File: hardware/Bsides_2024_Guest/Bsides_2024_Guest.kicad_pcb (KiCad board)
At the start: 2 copper layers, 134.5 x 129.5 mm, 45 parts, among them J1 Add_On, J2 Battery, J3 Battery, J4 OLED, J5 Conn_01x05, J6 Conn_01x05, P1 USB_C_Plug_USB2.0, Q1 DMG3415U-7, SW1 ON, SW2 RESET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

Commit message: feat(Hw): Update PCB
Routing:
- added copper zone on F.Cu, net (none)

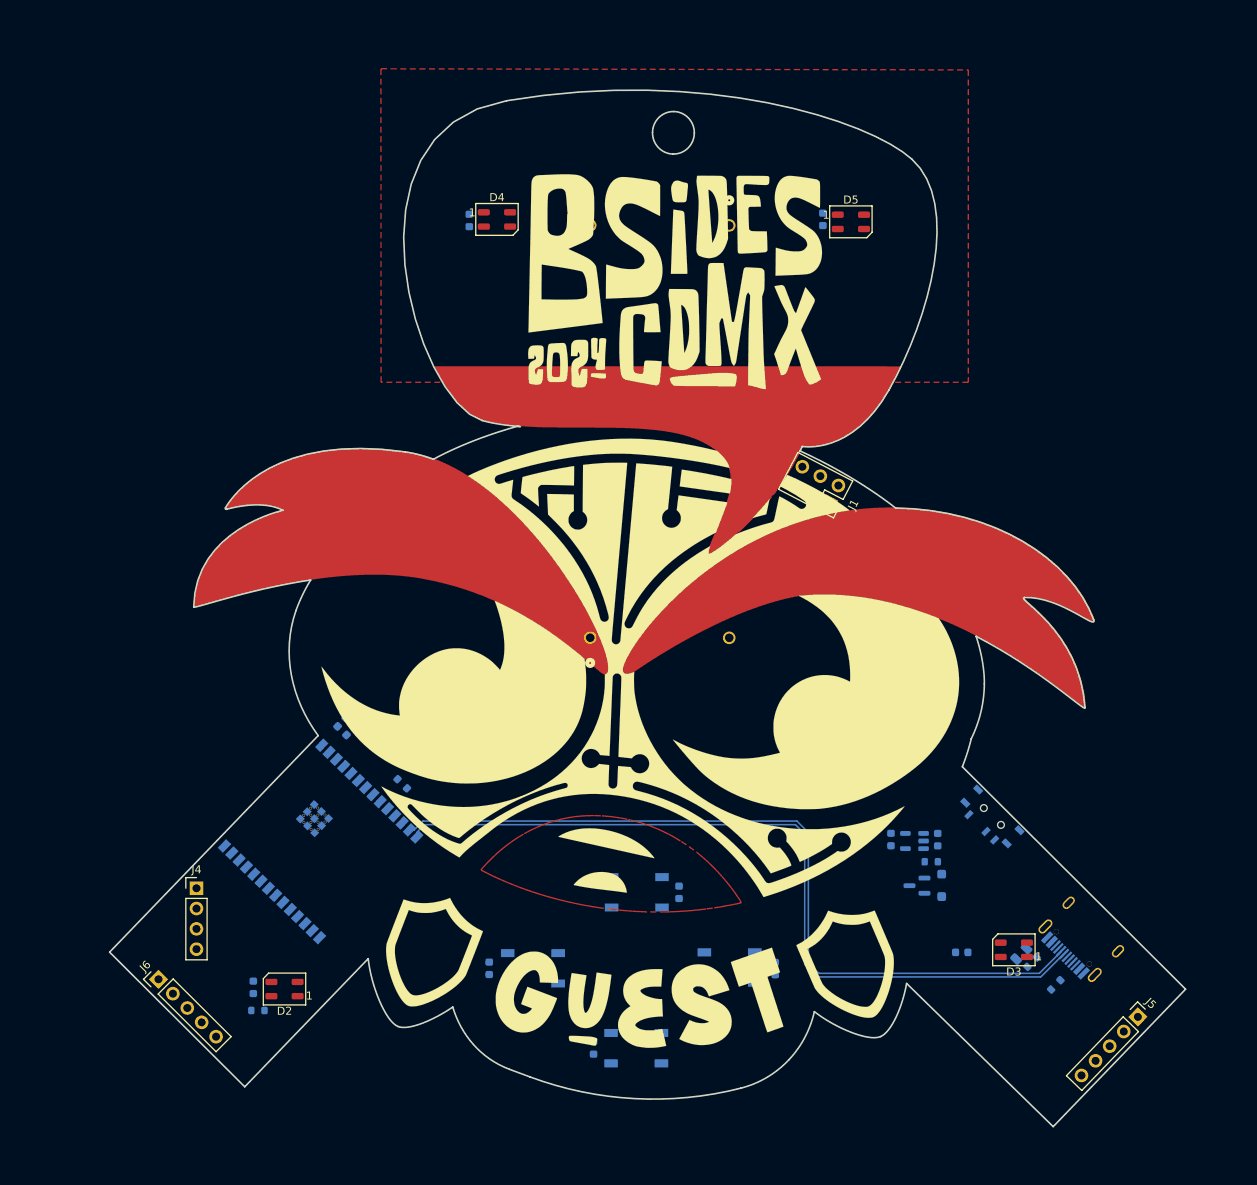
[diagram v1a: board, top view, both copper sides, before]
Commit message: Revert "Merge branch 'main' of https://github.com/ElectronicCats/badge-bsides-cdmx-2024"
This reverts commit 844f9cf1141b02d246949023f3a5d84c3d1d6870, reversing
changes made to df45190e2e7c4c17babbd6f5b24a18277498f0c6.
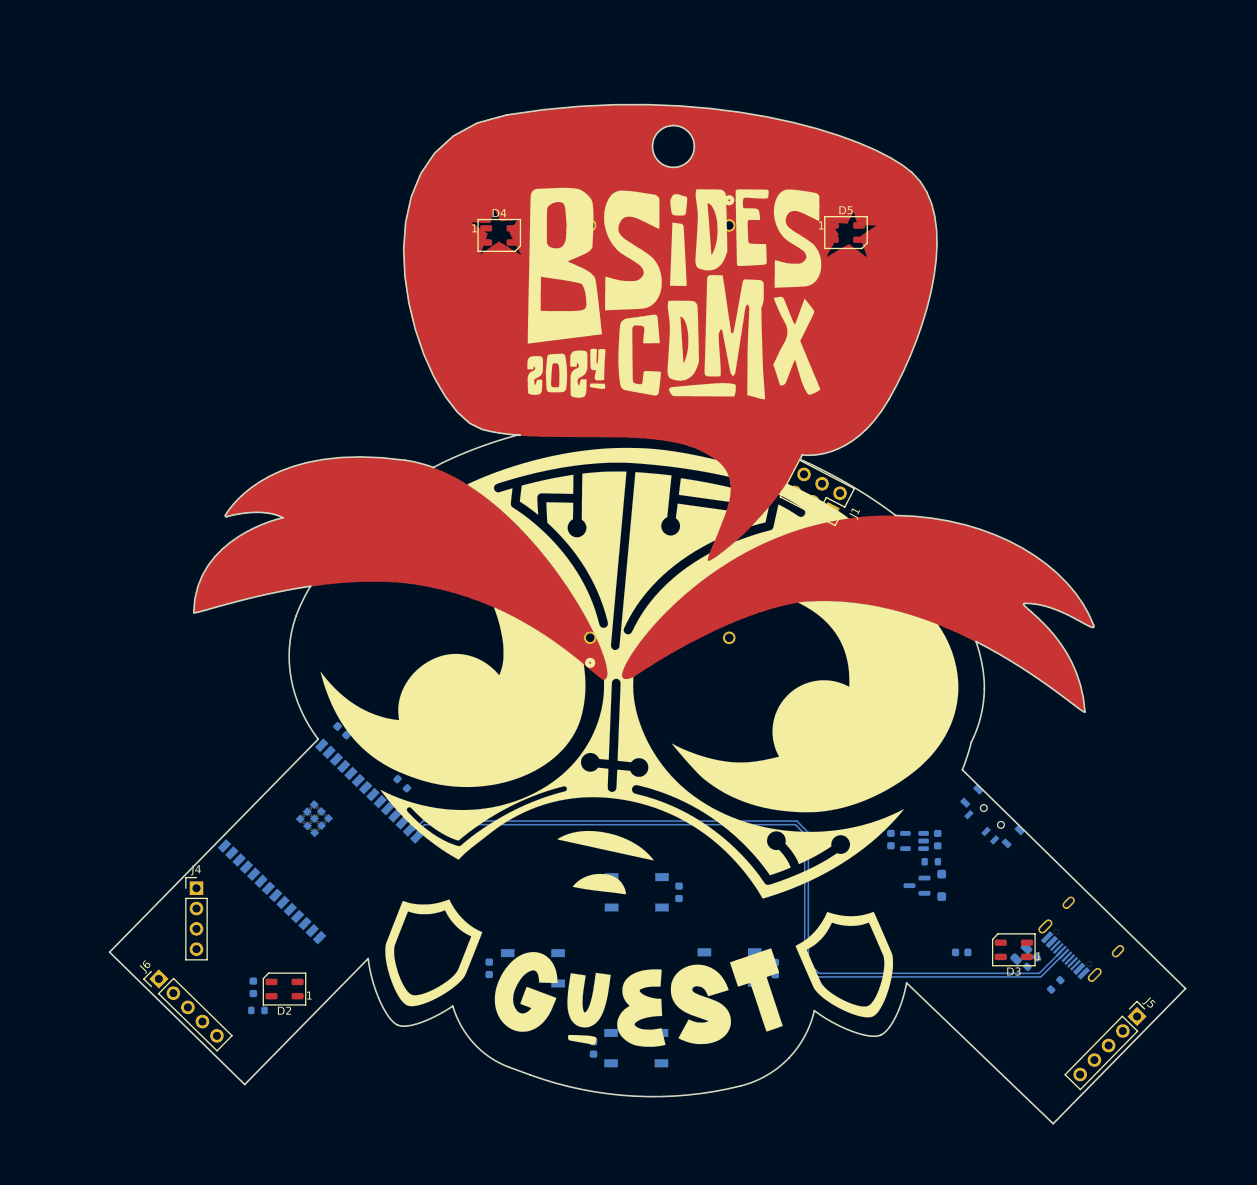
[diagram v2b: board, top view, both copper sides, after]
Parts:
- removed the Ref** at (125.1, 89.3)
- added Ref**: Val**, Guest:Badge Guest, F.Cu at (125.5, 89.8)
- J1: value Add_On -> Conn_02x03_Odd_Even
- moved C7 2.02 mm to (103.5, 42.5)
- moved D4 2.02 mm to (107.0, 42.4)
- moved C12 1.47 mm to (146.8, 41.7)
- moved D5 1.47 mm to (150.3, 42.0)
- moved J1 0.98 mm to (148.4, 76.9)
- moved J5 0.11 mm to (186.7, 140.0), turned to -44.407 degrees
- moved J6 0.07 mm to (64.4, 135.3), turned to 45.6 degrees
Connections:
- C1 pad 1: VBUS -> Net-(SW1-B)
- C12 pad 2: /VOUT -> +3V3
- C13 pad 1: /VOUT -> +3V3
- C14 pad 1: /VOUT -> +3V3
- C15 pad 1: /VOUT -> +3V3
- C2 pad 1: Net-(D1-A) -> +3V3
- C5 pad 2: /VOUT -> +3V3
- C6 pad 2: /VOUT -> +3V3
- C7 pad 2: /VOUT -> +3V3
- D1 pad 2: Net-(D1-A) -> VBUS
- D2 pad 1: /VOUT -> +3V3
- D3 pad 1: /VOUT -> +3V3
- D4 pad 1: /VOUT -> +3V3
- D5 pad 1: /VOUT -> +3V3
- J1 pad 1: /VOUT -> unconnected-(J1-Pin_1-Pad1)
- J1 pad 2: GND -> unconnected-(J1-Pin_2-Pad2)
- J1 pad 3: /SDA -> unconnected-(J1-Pin_3-Pad3)
- J1 pad 4: /SCL -> unconnected-(J1-Pin_4-Pad4)
- J4 pad 1: /VOUT -> +3V3
- Q1 pad 1: Net-(D1-A) -> VBUS
- R1 pad 2: /VOUT -> +3V3
- R2 pad 1: Net-(D1-A) -> VBUS
- R5 pad 2: /VOUT -> +3V3
- SW1 pad 2: /VOUT -> Net-(SW1-B)
- U1 pad 2: /VOUT -> +3V3
- U2 pad 1: VBUS -> Net-(SW1-B)
- U2 pad 3: VBUS -> Net-(SW1-B)
- U2 pad 5: Net-(D1-A) -> +3V3
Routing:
- removed copper zone on F.Cu, net (none)
- removed copper zone on F.Cu, net GND
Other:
- board size 134.5 x 129.5 mm -> 134.5 x 127.4 mm

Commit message: feat(Hw): Update PCB
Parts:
- removed the Ref** at (125.5, 89.8)
- added Ref**: Val**, Guest:Badge_Guest_Bsides_2024_CDMX (1), F.Cu at (125.1, 89.3)
- J1: value Conn_02x03_Odd_Even -> Add_On
- moved J1 6.52 mm to (145.1, 71.2), turned to 62.5 degrees
- moved C7 2.02 mm to (103.2, 40.5)
- moved D4 2.02 mm to (106.7, 40.4)
- moved C12 1.47 mm to (147.4, 40.4)
- moved D5 1.47 mm to (150.9, 40.7)
- moved J5 0.11 mm to (186.8, 140.1), turned to -43.926 degrees
- moved J6 0.07 mm to (64.4, 135.4), turned to 45.111 degrees
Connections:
- C1 pad 1: Net-(SW1-B) -> VBUS
- C12 pad 2: +3V3 -> /VOUT
- C13 pad 1: +3V3 -> /VOUT
- C14 pad 1: +3V3 -> /VOUT
- C15 pad 1: +3V3 -> /VOUT
- C2 pad 1: +3V3 -> Net-(D1-A)
- C5 pad 2: +3V3 -> /VOUT
- C6 pad 2: +3V3 -> /VOUT
- C7 pad 2: +3V3 -> /VOUT
- D1 pad 2: VBUS -> Net-(D1-A)
- D2 pad 1: +3V3 -> /VOUT
- D3 pad 1: +3V3 -> /VOUT
- D4 pad 1: +3V3 -> /VOUT
- D5 pad 1: +3V3 -> /VOUT
- J1 pad 1: unconnected-(J1-Pin_1-Pad1) -> /VOUT
- J1 pad 2: unconnected-(J1-Pin_2-Pad2) -> GND
- J1 pad 3: unconnected-(J1-Pin_3-Pad3) -> /SDA
- J1 pad 4: unconnected-(J1-Pin_4-Pad4) -> /SCL
- J4 pad 1: +3V3 -> /VOUT
- Q1 pad 1: VBUS -> Net-(D1-A)
- R1 pad 2: +3V3 -> /VOUT
- R2 pad 1: VBUS -> Net-(D1-A)
- R5 pad 2: +3V3 -> /VOUT
- SW1 pad 2: Net-(SW1-B) -> /VOUT
- U1 pad 2: +3V3 -> /VOUT
- U2 pad 1: Net-(SW1-B) -> VBUS
- U2 pad 3: Net-(SW1-B) -> VBUS
- U2 pad 5: +3V3 -> Net-(D1-A)
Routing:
- added copper zone on F.Cu, net (none)
- added copper zone on F.Cu, net GND
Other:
- board size 134.5 x 127.4 mm -> 134.5 x 129.5 mm

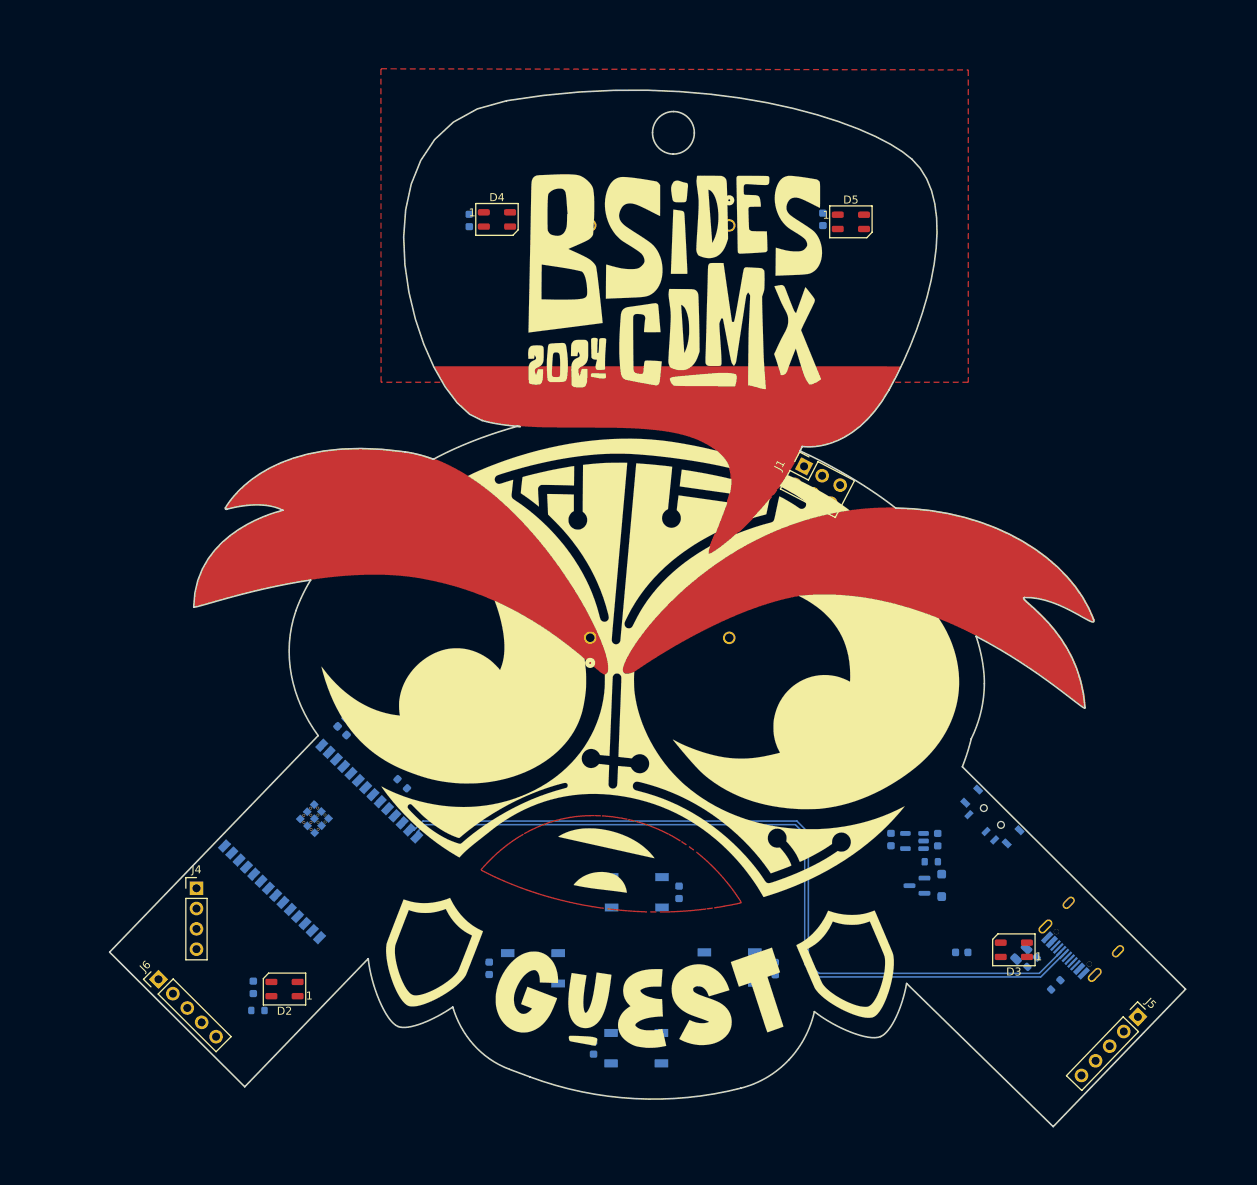
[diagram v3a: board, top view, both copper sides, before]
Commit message: feat(Hw): Update route
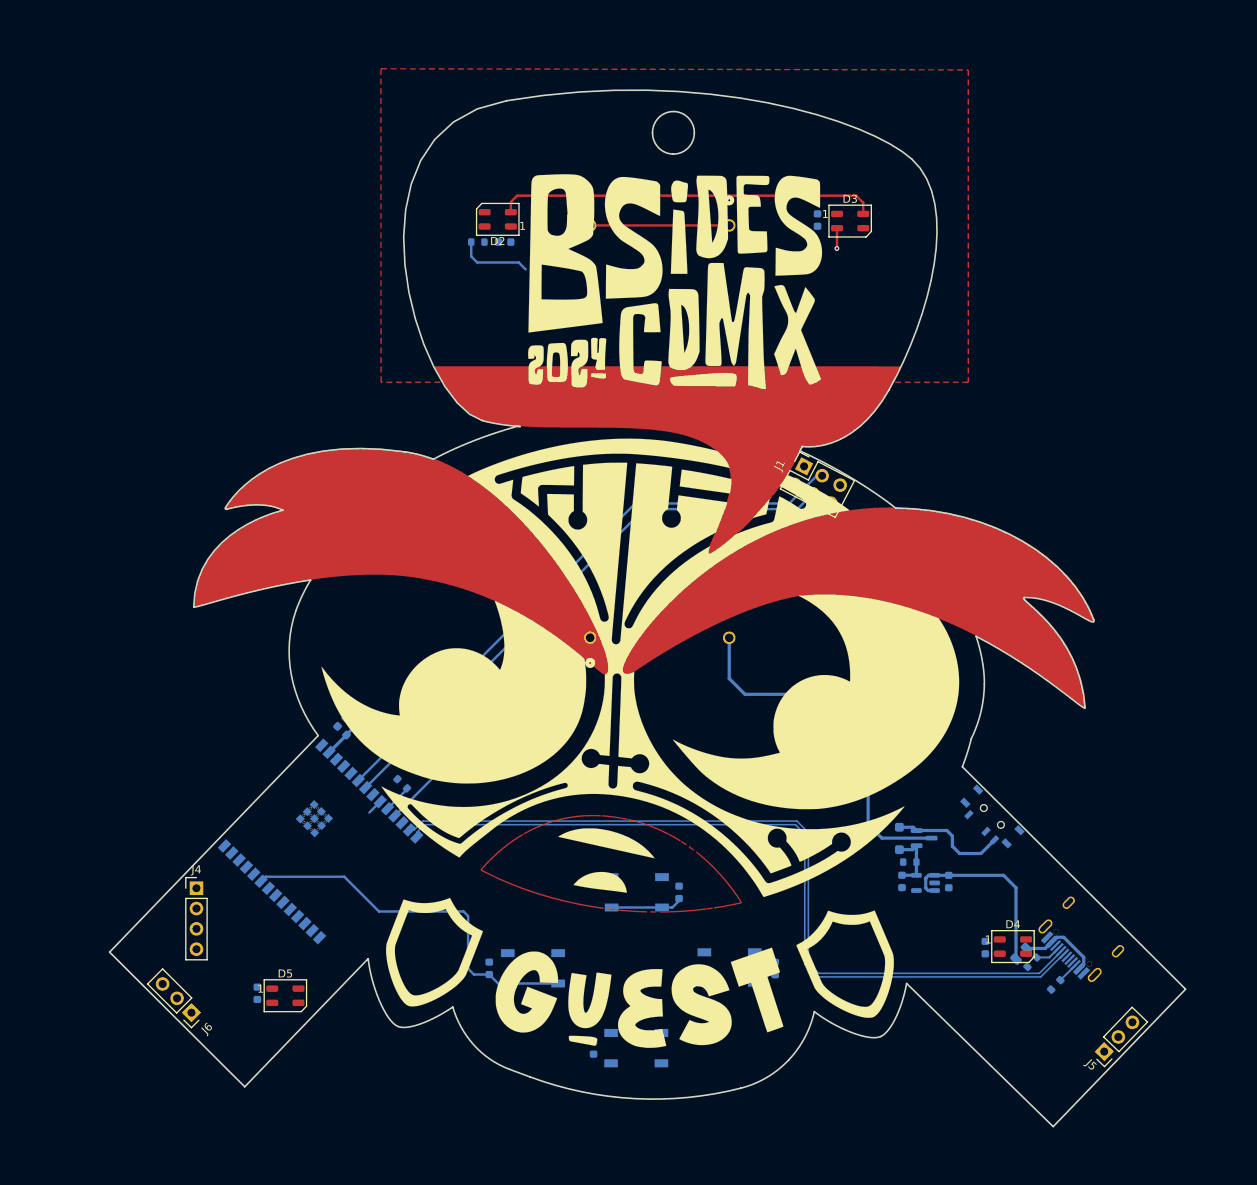
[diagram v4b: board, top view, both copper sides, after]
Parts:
- J5: value Conn_01x05 -> Serial_IN; footprint Connector_PinHeader_2.54mm:PinHeader_1x05_P2.54mm_Vertical -> Connector_PinHeader_2.54mm:PinHeader_1x03_P2.54mm_Vertical
- J6: value Conn_01x05 -> Serial_OUT; footprint Connector_PinHeader_2.54mm:PinHeader_1x05_P2.54mm_Vertical -> Connector_PinSocket_2.54mm:PinSocket_1x03_P2.54mm_Vertical
- moved C12 119.8 mm to (76.7, 137.1)
- moved D5 119.8 mm to (80.2, 137.4)
- moved C7 111.5 mm to (167.7, 131.4)
- moved D4 111.5 mm to (171.2, 131.3)
- moved R6 99.9 mm to (104.3, 43.2), turned to 0 degrees
- moved D2 99.8 mm to (106.8, 40.4)
- moved C5 98.3 mm to (107.6, 43.2), turned to 0 degrees
- moved D3 93.4 mm to (150.8, 40.6), turned to 0 degrees
- moved C6 93.3 mm to (146.7, 40.5), turned to 90 degrees
- moved D1 7.89 mm to (157.0, 117.8), turned to -90 degrees
- moved J5 6.04 mm to (182.6, 144.4), turned to 136.074 degrees
- moved Q1 6.01 mm to (160.1, 117.7), turned to 0 degrees
- moved J6 5.86 mm to (68.5, 139.5), turned to -134.889 degrees
- moved C2 5.42 mm to (157.3, 123.1)
- moved C1 5.42 mm to (163.2, 123.1)
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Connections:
- J1 pad 5: unconnected-(J1-Pin_5-Pad5) -> /GPIO3
- J1 pad 6: unconnected-(J1-Pin_6-Pad6) -> /GPIO2
- J4 pad 1: /VOUT -> /SDA
- J4 pad 2: GND -> /SCL
- J4 pad 3: /SCL -> /VOUT
- J4 pad 4: /SDA -> GND
- J5 pad 1: unconnected-(J5-Pin_1-Pad1) -> /GPIO16
- J5 pad 2: unconnected-(J5-Pin_2-Pad2) -> /GPIO17
- J5 pad 3: unconnected-(J5-Pin_3-Pad3) -> GND
- J6 pad 1: unconnected-(J6-Pin_1-Pad1) -> /GPIO4
- J6 pad 2: unconnected-(J6-Pin_2-Pad2) -> /GPIO5
- J6 pad 3: unconnected-(J6-Pin_3-Pad3) -> GND
- R1 pad 1: /PIN -> Net-(U1-IO8)
- U1 pad 10: /PIN -> Net-(U1-IO8)
- U1 pad 11: unconnected-(U1-IO10-Pad11) -> /PIN
- U1 pad 24: /RX -> /GPIO17
- U1 pad 25: /TX -> /GPIO16
- U1 pad 26: unconnected-(U1-IO3-Pad26) -> /GPIO3
- U1 pad 27: unconnected-(U1-IO2-Pad27) -> /GPIO2
- U1 pad 4: unconnected-(U1-IO4-Pad4) -> /GPIO4
- U1 pad 5: unconnected-(U1-IO5-Pad5) -> /GPIO5
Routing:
- net /SDA: track 0.00 -> 73.8 mm
- net /SCL: track 0.00 -> 71.1 mm
- net Net-(D2-DOUT): track 0.00 -> 47.4 mm
- net +BATT: track 0.00 -> 47.0 mm
- net /GPIO15: track 0.00 -> 46.8 mm
- net /PIN: track 0.00 -> 32.4 mm
- net VBUS: track 0.00 -> 23.5 mm
- net Net-(J2-Pin_1): track 0.00 -> 17.4 mm
- net Net-(D1-K): track 0.00 -> 14.7 mm
- net /GPIO1: track 0.00 -> 11.0 mm
- net Net-(F1-Pad1): track 0.00 -> 10.5 mm
- net Net-(D1-A): track 0.00 -> 7.87 mm
- net /VOUT: track 0.00 -> 6.05 mm
- net Net-(U1-IO8): track 0.00 -> 3.56 mm
- net Net-(P1-CC): track 0.00 -> 3.18 mm
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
